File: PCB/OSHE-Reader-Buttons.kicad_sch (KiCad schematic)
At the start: 10 parts, among them SW1 SW_Push, SW2 SW_Push, SW3 SW_Push, SW4 SW_Push, SW5 SW_Push

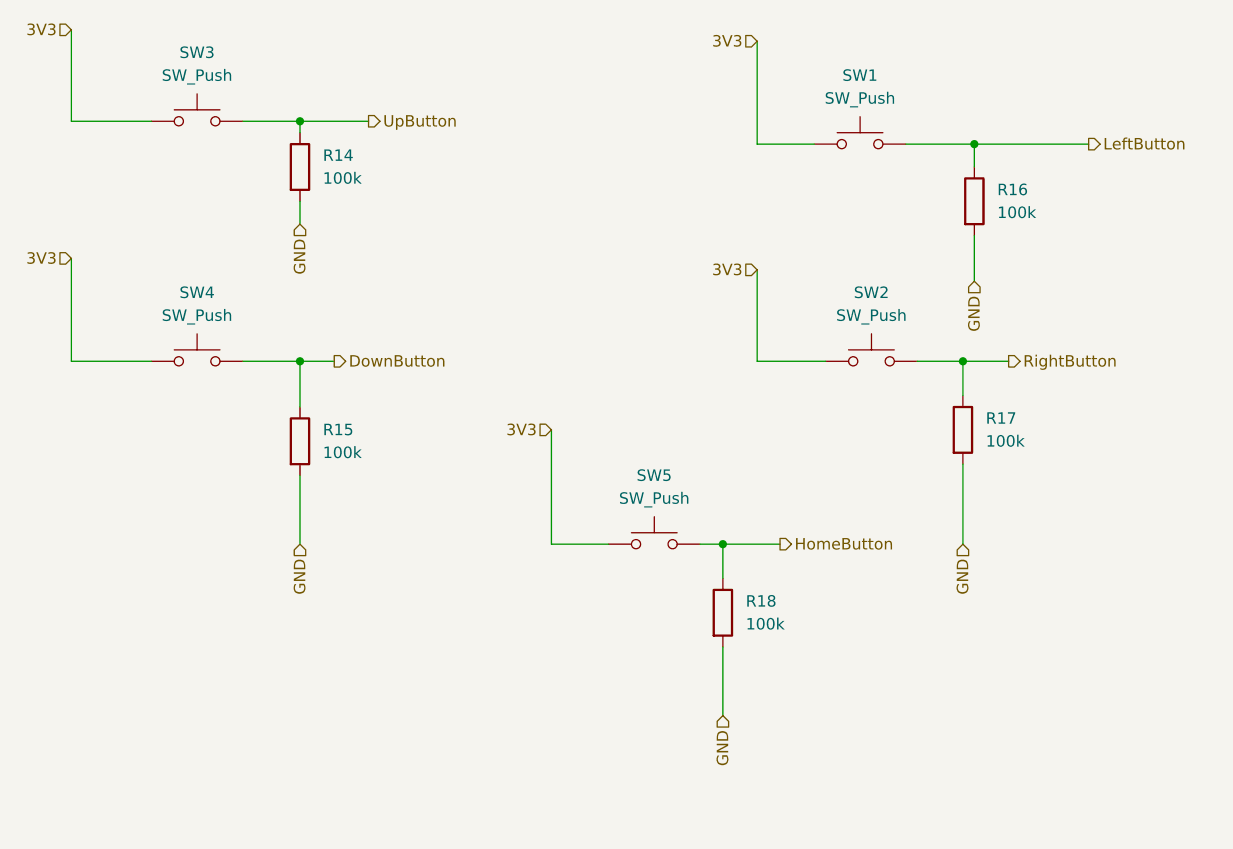
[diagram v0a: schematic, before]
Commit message: Added a bunch of test points to schematic and pcb, hopefully not needed, but good to have :)
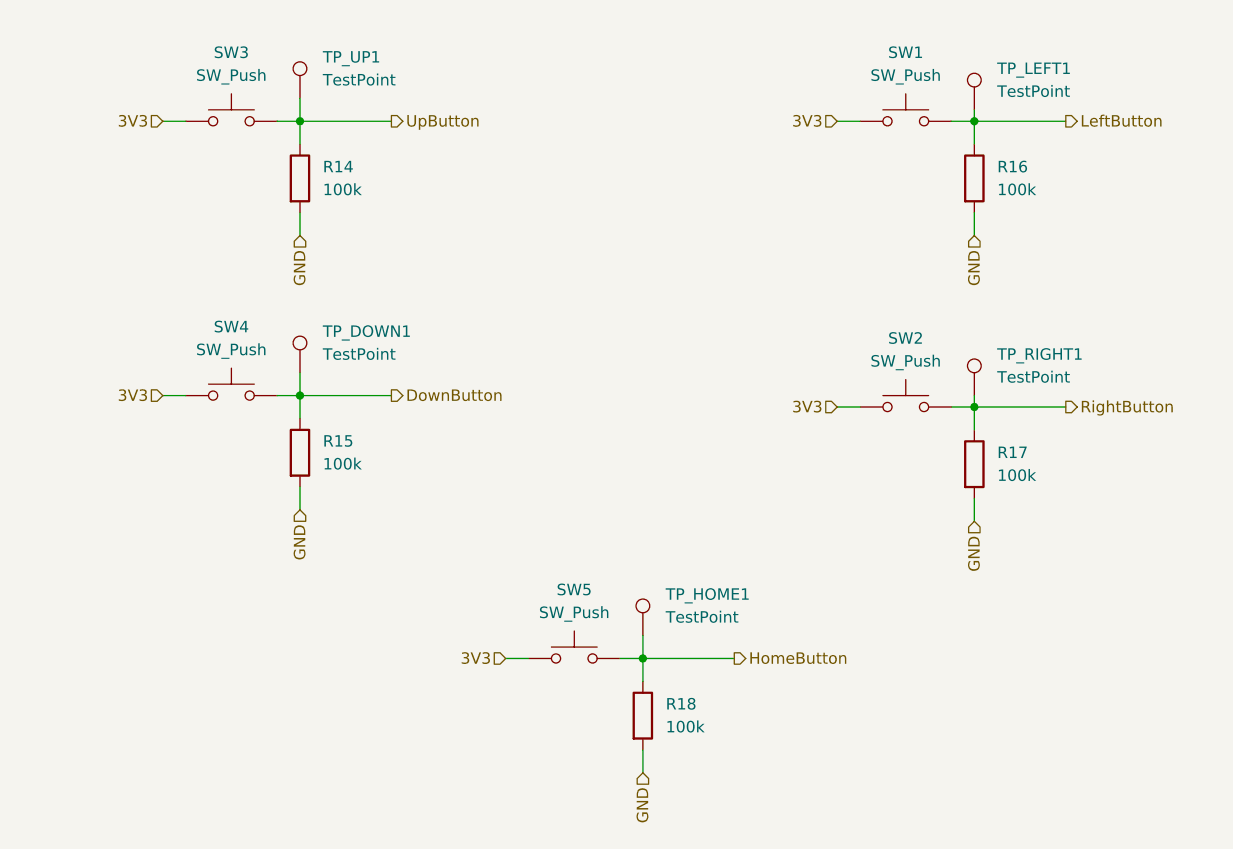
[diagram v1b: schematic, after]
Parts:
- added TP_DOWN1, TP_HOME1, TP_LEFT1, TP_RIGHT1, TP_UP1: TestPoint, TestPoint:TestPoint_Keystone_5019_Miniature, symbol Connector:TestPoint
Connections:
- net DownButton: now also TP_DOWN1.1
- net HomeButton: now also TP_HOME1.1
- net LeftButton: now also TP_LEFT1.1
- net RightButton: now also TP_RIGHT1.1
- net UpButton: now also TP_UP1.1
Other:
- moved on the sheet: R14, R15, R16, R17, R18, SW1, SW2, SW3, SW4, SW5
